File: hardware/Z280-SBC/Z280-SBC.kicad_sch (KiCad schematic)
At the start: 17 parts, among them Q1 2N7002, SW1 RESET, U1 74HC14, U2 Z280CPU, U3 74HC573, U4 74HC573, Y1 Crystal, Y2 Crystal

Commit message: Fixed most of the issues with Rev.1
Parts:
- added JP7: ~{AOE} AUTO, Jumper:SolderJumper-2_P1.3mm_Bridged_RoundedPad1.0x1.5mm, symbol Jumper:SolderJumper_2_Bridged
- added Q2: 2N7002, Package_TO_SOT_SMD:SOT-23, symbol Transistor_FET:2N7002
- added R5: 10k, Resistor_THT:R_Axial_DIN0204_L3.6mm_D1.6mm_P5.08mm_Horizontal, symbol Device:R_Small
- C2, C3: value ??pF -> 20pF
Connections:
- net ALT_CLK is gone; now on net CTIN1: R4.1, U1.12, Y2.2
- net +5V: now also R5.1
- net GND: now also Q2.2 (S)
- net ~{AS}: now also U1.3; no longer U3.11 (Load), U4.11 (Load)
- net ~{BUSACK}: now also JP7.2 (B); no longer U1.3
- net at JP1.2 (B): now also Q2.3 (D), R5.2; no longer U1.4
- new net: JP7.1 (A), Q2.1 (G)
- new net ALE: U1.4, U3.11 (Load), U4.11 (Load)
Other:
- note added: "ADDRESS LATCH CONTROL"
- note added: "POWER-ON RESET CONTROL"
- note added: "SERIAL CLOCK"
- moved on the sheet: JP1, R3, R4, U1B, U1E, U1F, Y2

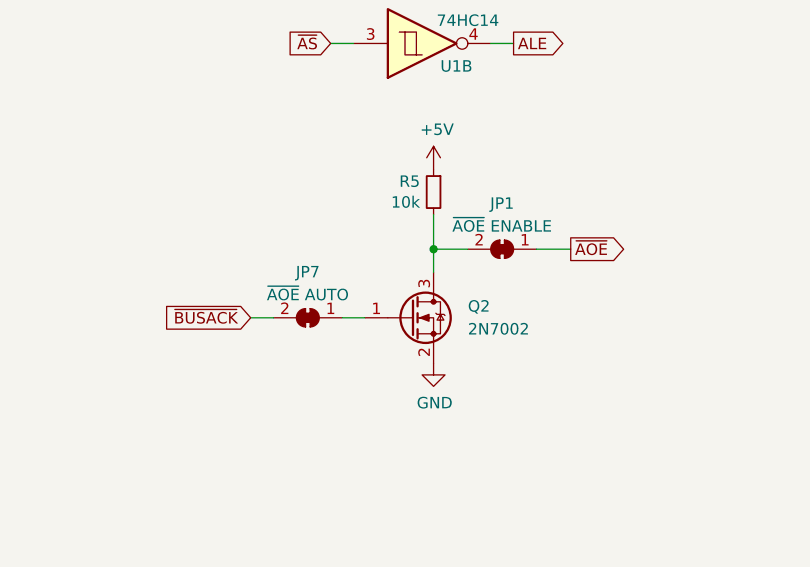
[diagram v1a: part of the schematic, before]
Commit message: Added computie-kicad-library and fixed references to point to it
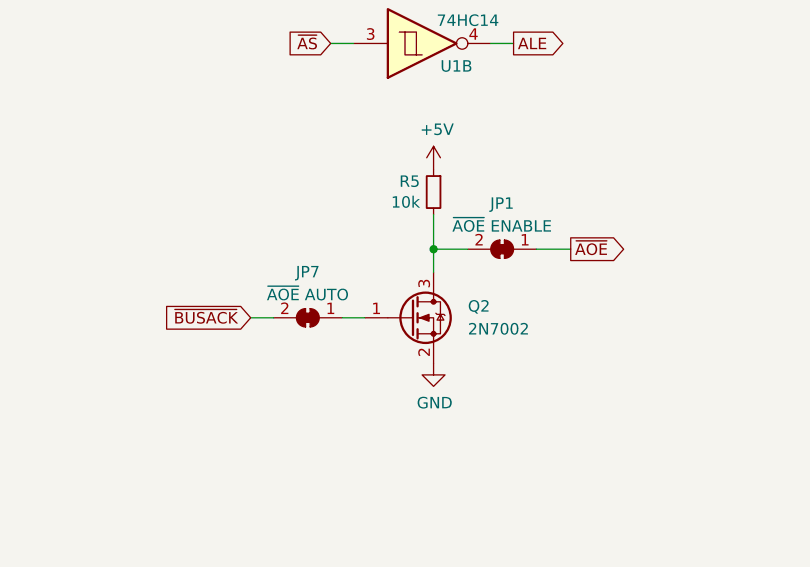
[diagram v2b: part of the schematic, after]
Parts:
- U2: symbol Z280:Z280CPU -> Computie_Z280:Z280CPU
